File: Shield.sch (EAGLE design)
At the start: 50 parts

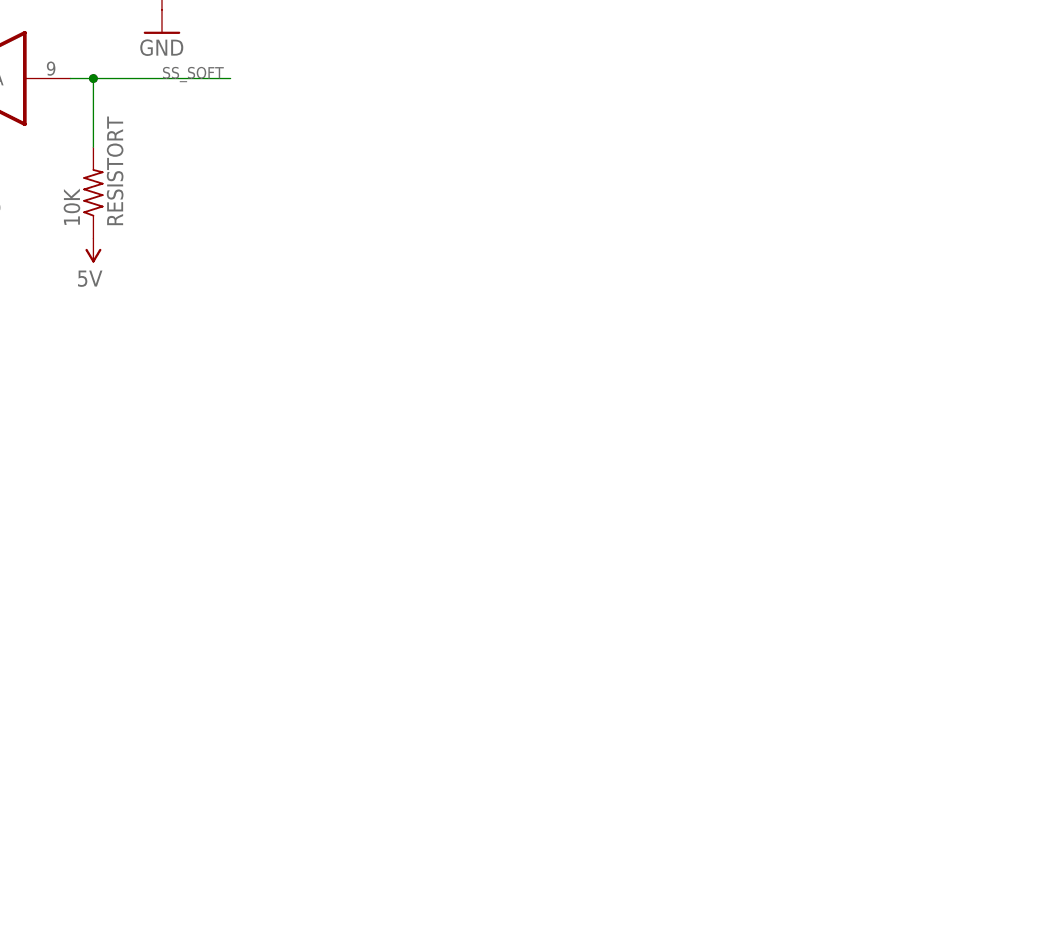
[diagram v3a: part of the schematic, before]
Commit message: Added ADS7841
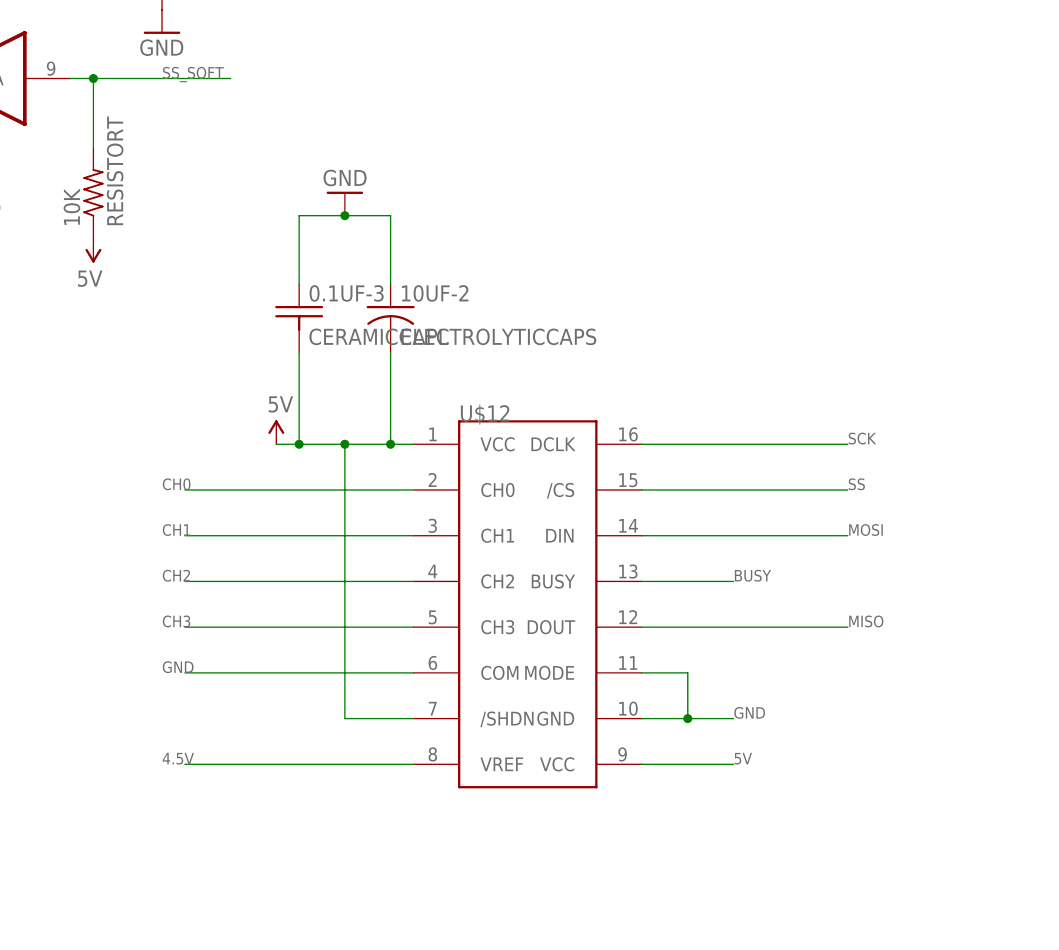
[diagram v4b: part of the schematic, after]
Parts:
- added 0.1UF-3: CERAMICCAPL, LEMS:CERAMICCAPL
- added 10UF-2: ELECTROLYTICCAPS, LEMS:ELECTROLYTICCAPS
- added U$12: ADS7841P, LEMS:ADS7841P
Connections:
- new net BUSY: U$12.BUSY
- new net CH0: U$12.CH0
- new net CH1: U$12.CH1
- new net CH2: U$12.CH2
- new net CH3: U$12.CH3
- net 4.5V: now also U$12.VREF
- net 5V: now also 0.1UF-3.2, 10UF-2.2, U$12./SHDN, U$12.VCC, U$12.VCC@2
- net GND: now also 0.1UF-3.1, 10UF-2.1, U$12.COM, U$12.GND, U$12.MODE
- net MISO: now also U$12.DOUT
- net MOSI: now also U$12.DIN
- net SCK: now also U$12.DCLK
- net SS: now also U$12./CS
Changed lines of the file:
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@@
 <part name="GND14" library="LEMS" deviceset="GND" device=""/>
 <part name="AREFJUMPER" library="LEMS" deviceset="JUMPER2PIN" device="N"/>
+<part name="U$12" library="LEMS" deviceset="ADS7841" device="P"/>
+<part name="U$13" library="LEMS" deviceset="5V" device=""/>
+<part name="0.1UF-3" library="LEMS" deviceset="CERAMICCAP" device="L"/>
+<part name="10UF-2" library="LEMS" deviceset="ELECTROLYTICCAP" device="S"/>
+<part name="GND15" library="LEMS" deviceset="GND" device=""/>
 </parts>
 <sheets>
@@
 <instance part="GND14" gate="1" x="78.74" y="50.8"/>
 <instance part="AREFJUMPER" gate="G$1" x="27.94" y="20.32"/>
+<instance part="U$12" gate="ADS7841" x="165.1" y="71.12"/>
+<instance part="U$13" gate="G$1" x="137.16" y="88.9"/>
+<instance part="0.1UF-3" gate="G$1" x="139.7" y="104.14"/>
+<instance part="10UF-2" gate="G$1" x="149.86" y="104.14"/>
+<instance part="GND15" gate="1" x="144.78" y="116.84" rot="R180"/>
 </instances>
 <busses>
@@
 <pinref part="GND14" gate="1" pin="GND"/>
 </segment>
+<segment>
+<pinref part="0.1UF-3" gate="G$1" pin="1"/>
+<wire x1="139.7" y1="106.68" x2="139.7" y2="114.3" width="0.1524" layer="91"/>
+<pinref part="10UF-2" gate="G$1" pin="1"/>
+<wire x1="139.7" y1="114.3" x2="144.78" y2="114.3" width="0.1524" layer="91"/>
+<wire x1="144.78" y1="114.3" x2="149.86" y2="114.3" width="0.1524" layer="91"/>
+<wire x1="149.86" y1="114.3" x2="149.86" y2="106.68" width="0.1524" layer="91"/>
+<pinref part="GND15" gate="1" pin="GND"/>
+<junction x="144.78" y="114.3"/>
+</segment>
+<segment>
+<pinref part="U$12" gate="ADS7841" pin="COM"/>
+<wire x1="152.4" y1="63.5" x2="127" y2="63.5" width="0.1524" layer="91"/>
+<label x="124.46" y="63.5" size="1.27" layer="95"/>
+</segment>
+<segment>
+<pinref part="U$12" gate="ADS7841" pin="GND"/>
+<wire x1="177.8" y1="58.42" x2="182.88" y2="58.42" width="0.1524" layer="91"/>
+<label x="187.96" y="58.42" size="1.27" layer="95"/>
+<pinref part="U$12" gate="ADS7841" pin="MODE"/>
+<wire x1="182.88" y1="58.42" x2="187.96" y2="58.42" width="0.1524" layer="91"/>
+<wire x1="177.8" y1="63.5" x2="182.88" y2="63.5" width="0.1524" layer="91"/>
+<wire x1="182.88" y1="63.5" x2="182.88" y2="58.42" width="0.1524" layer="91"/>
+<junction x="182.88" y="58.42"/>
+</segment>
 </net>
 <net name="MOSI_SOFT" class="0">
@@
 <label x="22.86" y="66.04" size="1.27" layer="95"/>
 </segment>
+<segment>
+<pinref part="U$12" gate="ADS7841" pin="VCC"/>
+<wire x1="152.4" y1="88.9" x2="149.86" y2="88.9" width="0.1524" layer="91"/>
+<pinref part="U$13" gate="G$1" pin="5V"/>
+<pinref part="0.1UF-3" gate="G$1" pin="2"/>
+<wire x1="149.86" y1="88.9" x2="144.78" y2="88.9" width="0.1524" layer="91"/>
+<wire x1="144.78" y1="88.9" x2="139.7" y2="88.9" width="0.1524" layer="91"/>
+<wire x1="139.7" y1="88.9" x2="137.16" y2="88.9" width="0.1524" layer="91"/>
+<wire x1="139.7" y1="88.9" x2="139.7" y2="99.06" width="0.1524" layer="91"/>
+<junction x="139.7" y="88.9"/>
+<pinref part="10UF-2" gate="G$1" pin="2"/>
+<wire x1="149.86" y1="88.9" x2="149.86" y2="99.06" width="0.1524" layer="91"/>
+<junction x="149.86" y="88.9"/>
+<pinref part="U$12" gate="ADS7841" pin="/SHDN"/>
+<wire x1="152.4" y1="58.42" x2="144.78" y2="58.42" width="0.1524" layer="91"/>
+<wire x1="144.78" y1="58.42" x2="144.78" y2="88.9" width="0.1524" layer="91"/>
+<junction x="144.78" y="88.9"/>
+</segment>
+<segment>
+<pinref part="U$12" gate="ADS7841" pin="VCC@2"/>
+<wire x1="177.8" y1="53.34" x2="187.96" y2="53.34" width="0.1524" layer="91"/>
+<label x="187.96" y="53.34" size="1.27" layer="95"/>
+</segment>
 </net>
 <net name="I2C-2" class="0">
@@
 <label x="335.28" y="121.92" size="1.27" layer="95"/>
 </segment>
+<segment>
+<pinref part="U$12" gate="ADS7841" pin="DIN"/>
+<wire x1="177.8" y1="78.74" x2="200.66" y2="78.74" width="0.1524" layer="91"/>
+<label x="200.66" y="78.74" size="1.27" layer="95"/>
+</segment>
 </net>
 <net name="SS" class="0">
@@
 <label x="276.86" y="119.38" size="1.27" layer="95"/>
 </segment>
+<segment>
+<pinref part="U$12" gate="ADS7841" pin="/CS"/>
+<wire x1="177.8" y1="83.82" x2="200.66" y2="83.82" width="0.1524" layer="91"/>
+<label x="200.66" y="83.82" size="1.27" layer="95"/>
+</segment>
 </net>
 <net name="D22" class="0">
@@
 <label x="335.28" y="124.46" size="1.27" layer="95"/>
 </segment>
+<segment>
+<pinref part="U$12" gate="ADS7841" pin="DOUT"/>
+<wire x1="177.8" y1="68.58" x2="200.66" y2="68.58" width="0.1524" layer="91"/>
+<label x="200.66" y="68.58" size="1.27" layer="95"/>
+</segment>
 </net>
 <net name="SCK" class="0">
@@
 <wire x1="327.66" y1="119.38" x2="337.82" y2="119.38" width="0.1524" layer="91"/>
 <label x="335.28" y="119.38" size="1.27" layer="95"/>
+</segment>
+<segment>
+<pinref part="U$12" gate="ADS7841" pin="DCLK"/>
+<wire x1="177.8" y1="88.9" x2="200.66" y2="88.9" width="0.1524" layer="91"/>
+<label x="200.66" y="88.9" size="1.27" layer="95"/>
 </segment>
 </net>
@@
 <label x="12.7" y="17.78" size="1.27" layer="95"/>
 </segment>
-</net>
+<segment>
+<pinref part="U$12" gate="ADS7841" pin="VREF"/>
+<wire x1="152.4" y1="53.34" x2="127" y2="53.34" width="0.1524" layer="91"/>
+<label x="124.46" y="53.34" size="1.27" layer="95"/>
+</segment>
+</net>
+<net name="CH0" class="0">
+<segment>
+<pinref part="U$12" gate="ADS7841" pin="CH0"/>
+<wire x1="152.4" y1="83.82" x2="127" y2="83.82" width="0.1524" layer="91"/>
+<label x="124.46" y="83.82" size="1.27" layer="95"/>
+</segment>
+</net>
+<net name="CH1" class="0">
+<segment>
+<pinref part="U$12" gate="ADS7841" pin="CH1"/>
+<wire x1="152.4" y1="78.74" x2="127" y2="78.74" width="0.1524" layer="91"/>
+<label x="124.46" y="78.74" size="1.27" layer="95"/>
+</segment>
+</net>
+<net name="CH2" class="0">
+<segment>
+<pinref part="U$12" gate="ADS7841" pin="CH2"/>
+<wire x1="152.4" y1="73.66" x2="127" y2="73.66" width="0.1524" layer="91"/>
+<label x="124.46" y="73.66" size="1.27" layer="95"/>
+</segment>
+</net>
+<net name="CH3" class="0">
+<segment>
+<pinref part="U$12" gate="ADS7841" pin="CH3"/>
+<wire x1="152.4" y1="68.58" x2="127" y2="68.58" width="0.1524" layer="91"/>
+<label x="124.46" y="68.58" size="1.27" layer="95"/>
+</segment>
+</net>
+<net name="BUSY" class="0">
+<segment>
+<pinref part="U$12" gate="ADS7841" pin="BUSY"/>
+<wire x1="177.8" y1="73.66" x2="187.96" y2="73.66" width="0.1524" layer="91"/>
+<label x="187.96" y="73.66" size="1.27" layer="95"/>
+</segment>
+</net>

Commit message: First Complete Schematic
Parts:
- added 0.1UF-4, 0.1UF-5, 1UF-2: CERAMICCAPL, LEMS:CERAMICCAPL
- added 250K: RESISTORN, LEMS:RESISTORN
- added 44.2K, U$16, U$20: RESISTORT, LEMS:RESISTORT
- added 6.8UF: ELECTROLYTICCAPS, LEMS:ELECTROLYTICCAPS
- added ADCTERM, DALLASTERM: 3PINHEADERS, LEMS:3PINHEADERS
- added OPA1TERM, U$17, U$21: 2PINHEADERS, LEMS:2PINHEADERS
- added OPA2TERM: 3PINHEADERN, LEMS:3PINHEADERN
- added PWRSWTCH: SWITCHSPDTN, LEMS:SWITCHSPDTN
- added U$14: TLV2372P, LEMS:TLV2372P
- added U$18: TPS7250D, LEMS:TPS7250D
- added U$19: ELECTROLYTICCAPL, LEMS:ELECTROLYTICCAPL
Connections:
- new net DALDATA: DALLASTERM.2, U$16.1
- new net LIOP-: 1UF-2.1, 44.2K.1, OPA1TERM.2, U$14TLV2372-1.-IN
- new net N$2: OPA2TERM.1, U$14TLV2372-2.+IN
- new net N$3: OPA2TERM.2, U$14TLV2372-2.-IN
- new net N$4: OPA2TERM.3, U$14TLV2372-2.OUT
- new net N$6: 250K.1, U$18.RESET
- new net N$7: U$19.2, U$20.2
- new net N$8: 0.1UF-5.1, PWRSWTCH.P, U$18.IN1, U$18.IN2
- new net PWRN: PWRSWTCH.O, U$21.2
- net 4.5V: now also U$17.1, U$17.2
- net 5V: now also 0.1UF-4.1, 250K.2, 6.8UF.1, DALLASTERM.3, U$14TLV2372-PWRN.VCC, U$16.2, U$18.OUT1, U$18.OUT2, U$18.SENSE, U$19.1
- net CH0: now also 1UF-2.2, 44.2K.2, U$14TLV2372-1.OUT
- net CH1: now also ADCTERM.3
- net CH2: now also ADCTERM.2
- net CH3: now also ADCTERM.1
- net GND: now also 0.1UF-4.2, 0.1UF-5.2, 6.8UF.2, DALLASTERM.1, OPA1TERM.1, U$14TLV2372-1.+IN, U$14TLV2372-PWRN.GND, U$18.EN, U$18.GND, U$20.1, U$21.1

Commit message: Added board
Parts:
- renumbered U$16 to 4.7K, U$20 to 1, U$21 to PWRTERM
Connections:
- removed net DALDATA: 4.7K.1, DALLASTERM.2
- new net N$5: GND.1, GND.2
- net D39: now also 4.7K.1, DALLASTERM.2
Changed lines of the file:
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@@
 <part name="OPA2TERM" library="LEMS" deviceset="3PINHEADER" device="N"/>
 <part name="DALLASTERM" library="LEMS" deviceset="3PINHEADER" device="S"/>
-<part name="U$16" library="LEMS" deviceset="RESISTOR" device="T"/>
+<part name="4.7K" library="LEMS" deviceset="RESISTOR" device="T"/>
 <part name="GND17" library="LEMS" deviceset="GND" device=""/>
 <part name="U$17" library="LEMS" deviceset="2PINHEADER" device="S"/>
@@
 <part name="GND19" library="LEMS" deviceset="GND" device=""/>
 <part name="U$19" library="LEMS" deviceset="ELECTROLYTICCAP" device="L"/>
-<part name="U$20" library="LEMS" deviceset="RESISTOR" device="T"/>
+<part name="1" library="LEMS" deviceset="RESISTOR" device="T"/>
 <part name="GND20" library="LEMS" deviceset="GND" device=""/>
 <part name="PWRSWTCH" library="LEMS" deviceset="SWITCHSPDT" device="N"/>
-<part name="U$21" library="LEMS" deviceset="2PINHEADER" device="S"/>
+<part name="PWRTERM" library="LEMS" deviceset="2PINHEADER" device="S"/>
 <part name="GND21" library="LEMS" deviceset="GND" device=""/>
 </parts>
@@
 <instance part="OPA2TERM" gate="G$1" x="228.6" y="86.36" rot="R90"/>
 <instance part="DALLASTERM" gate="G$1" x="322.58" y="147.32"/>
-<instance part="U$16" gate="G$1" x="345.44" y="147.32"/>
+<instance part="4.7K" gate="G$1" x="345.44" y="147.32"/>
 <instance part="GND17" gate="1" x="175.26" y="121.92"/>
 <instance part="U$17" gate="G$1" x="91.44" y="81.28" rot="R270"/>
@@
 <instance part="GND19" gate="1" x="233.68" y="43.18" rot="R270"/>
 <instance part="U$19" gate="G$1" x="264.16" y="71.12" rot="R90"/>
-<instance part="U$20" gate="G$1" x="274.32" y="71.12" rot="R180"/>
+<instance part="1" gate="G$1" x="274.32" y="71.12" rot="R180"/>
 <instance part="GND20" gate="1" x="281.94" y="71.12" rot="R90"/>
 <instance part="PWRSWTCH" gate="G$1" x="302.26" y="40.64"/>
-<instance part="U$21" gate="G$1" x="325.12" y="43.18"/>
+<instance part="PWRTERM" gate="G$1" x="325.12" y="43.18"/>
 <instance part="GND21" gate="1" x="337.82" y="38.1"/>
 </instances>
@@
 </segment>
 <segment>
-<pinref part="U$20" gate="G$1" pin="1"/>
+<pinref part="1" gate="G$1" pin="1"/>
 <pinref part="GND20" gate="1" pin="GND"/>
 </segment>
 <segment>
-<pinref part="U$21" gate="G$1" pin="1"/>
+<pinref part="PWRTERM" gate="G$1" pin="1"/>
 <wire x1="330.2" y1="40.64" x2="337.82" y2="40.64" width="0.1524" layer="91"/>
 <pinref part="GND21" gate="1" pin="GND"/>
@@
 <wire x1="327.66" y1="149.86" x2="350.52" y2="149.86" width="0.1524" layer="91"/>
 <label x="332.74" y="149.86" size="1.27" layer="95"/>
-<pinref part="U$16" gate="G$1" pin="2"/>
+<pinref part="4.7K" gate="G$1" pin="2"/>
 <wire x1="350.52" y1="149.86" x2="350.52" y2="147.32" width="0.1524" layer="91"/>
 </segment>
@@
 <label x="276.86" y="137.16" size="1.27" layer="95"/>
 </segment>
+<segment>
+<pinref part="DALLASTERM" gate="G$1" pin="2"/>
+<wire x1="327.66" y1="147.32" x2="337.82" y2="147.32" width="0.1524" layer="91"/>
+<label x="332.74" y="147.32" size="1.27" layer="95"/>
+<pinref part="4.7K" gate="G$1" pin="1"/>
+<wire x1="337.82" y1="147.32" x2="340.36" y2="147.32" width="0.1524" layer="91"/>
+<wire x1="337.82" y1="147.32" x2="337.82" y2="160.02" width="0.1524" layer="91"/>
+<junction x="337.82" y="147.32"/>
+</segment>
 </net>
 <net name="D41" class="0">
@@
 </segment>
 </net>
-<net name="DALDATA" class="0">
-<segment>
-<pinref part="DALLASTERM" gate="G$1" pin="2"/>
-<wire x1="327.66" y1="147.32" x2="340.36" y2="147.32" width="0.1524" layer="91"/>
-<label x="332.74" y="147.32" size="1.27" layer="95"/>
-<pinref part="U$16" gate="G$1" pin="1"/>
-</segment>
-</net>
 <net name="N$6" class="0">
 <segment>
@@
 <segment>
 <pinref part="U$19" gate="G$1" pin="2"/>
-<pinref part="U$20" gate="G$1" pin="2"/>
+<pinref part="1" gate="G$1" pin="2"/>
 </segment>
 </net>
 <net name="PWRN" class="0">
 <segment>
-<pinref part="U$21" gate="G$1" pin="2"/>
+<pinref part="PWRTERM" gate="G$1" pin="2"/>
 <wire x1="330.2" y1="43.18" x2="330.2" y2="50.8" width="0.1524" layer="91"/>
 <pinref part="PWRSWTCH" gate="G$1" pin="O"/>
@@
 </segment>
 </net>
+<net name="N$5" class="0">
+<segment>
+<pinref part="GND" gate="G$1" pin="1"/>
+<pinref part="GND" gate="G$1" pin="2"/>
+<wire x1="284.48" y1="99.06" x2="287.02" y2="99.06" width="0.1524" layer="91"/>
+</segment>
+</net>
